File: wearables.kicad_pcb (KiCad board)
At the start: 2 copper layers, 36 x 46.9 mm, 39 parts, among them P1 +, P2 +, P3 -, P4 -, P5 +, P6 -, SW1 ON|OFF

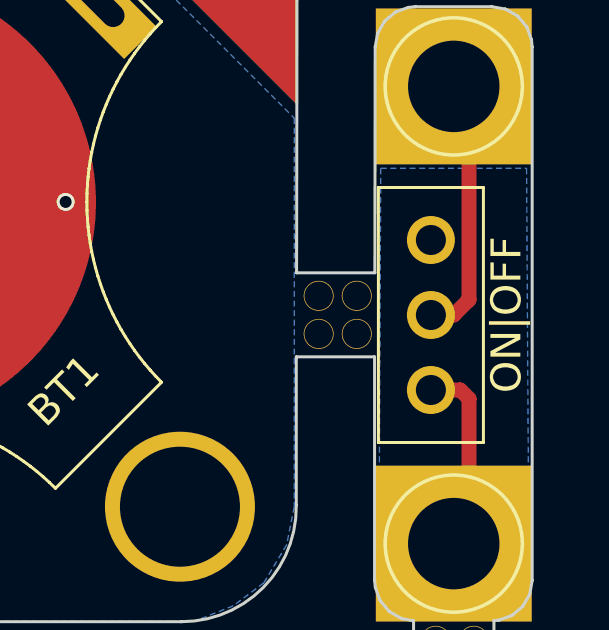
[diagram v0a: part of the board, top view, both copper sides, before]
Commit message: Moved switch over.
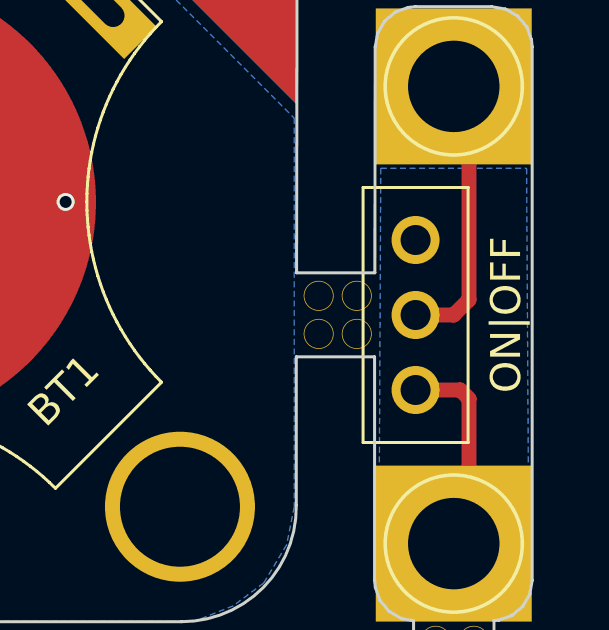
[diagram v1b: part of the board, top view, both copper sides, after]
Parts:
- moved SW1 0.51 mm to (51.5, 36.7)
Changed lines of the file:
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@@
     (links 36)
     (no_connects 12)
-    (area 17.81589 17.513889 55.805 66.001001)
+    (area 19.379388 18.783751 55.46939 65.799453)
     (thickness 1.6)
     (drawings 263)
@@
     (pcbplotparams
       (layerselection 0x010fc_80000001)
-      (usegerberextensions true)
+      (usegerberextensions false)
       (excludeedgelayer true)
       (linewidth 0.100000)
@@
       (padsonsilk false)
       (subtractmaskfromsilk false)
-      (outputformat 1)
+      (outputformat 3)
       (mirror false)
       (drillshape 0)
       (scaleselection 1)
-      (outputdirectory gerber/))
+      (outputdirectory dxf/))
   )
   (net 0 "")
@@
     (pad 2 smd circle (at -0.10922 -0.0884 90) (size 15 15) (layers F.Cu F.Paste F.Mask)
       (net 2 "Net-(BT1-Pad2)"))
+    (model ../../../../../../Users/mage/Desktop/CR2032-metal.wrl
+      (at (xyz 0 0 0))
+      (scale (xyz 10 10 10))
+      (rotate (xyz 0 0 0))
+    )
   )
   (module Connect:1pin (layer F.Cu)
@@
   )
   (module libs:SS12D00 (layer F.Cu)
-    (at 52.001041 36.689313 90)
+    (at 51.49 36.689313 90)
     (fp_text reference SW1 (at -5.0292 0.01016 180) (layer F.SilkS) hide
       (effects (font (size 0.8 0.8) (thickness 0.12)))
     )
-    (fp_text value ON|OFF (at 0.009313 2.518959 90) (layer F.SilkS)
-      (effects (font (size 1 1) (thickness 0.15)))
-    )
+    (fp_text value ON|OFF (at 0.009313 3.02 90) (layer F.SilkS)
+      (effects (font (size 1 1) (thickness 0.15)))
+    )
